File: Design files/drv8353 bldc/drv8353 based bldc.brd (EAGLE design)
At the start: 127 x 127 mm, 112 parts, among them IC1 DRV8353RSRGZT, J3 2X6 FEMALE, J4 B06B-HCMKK

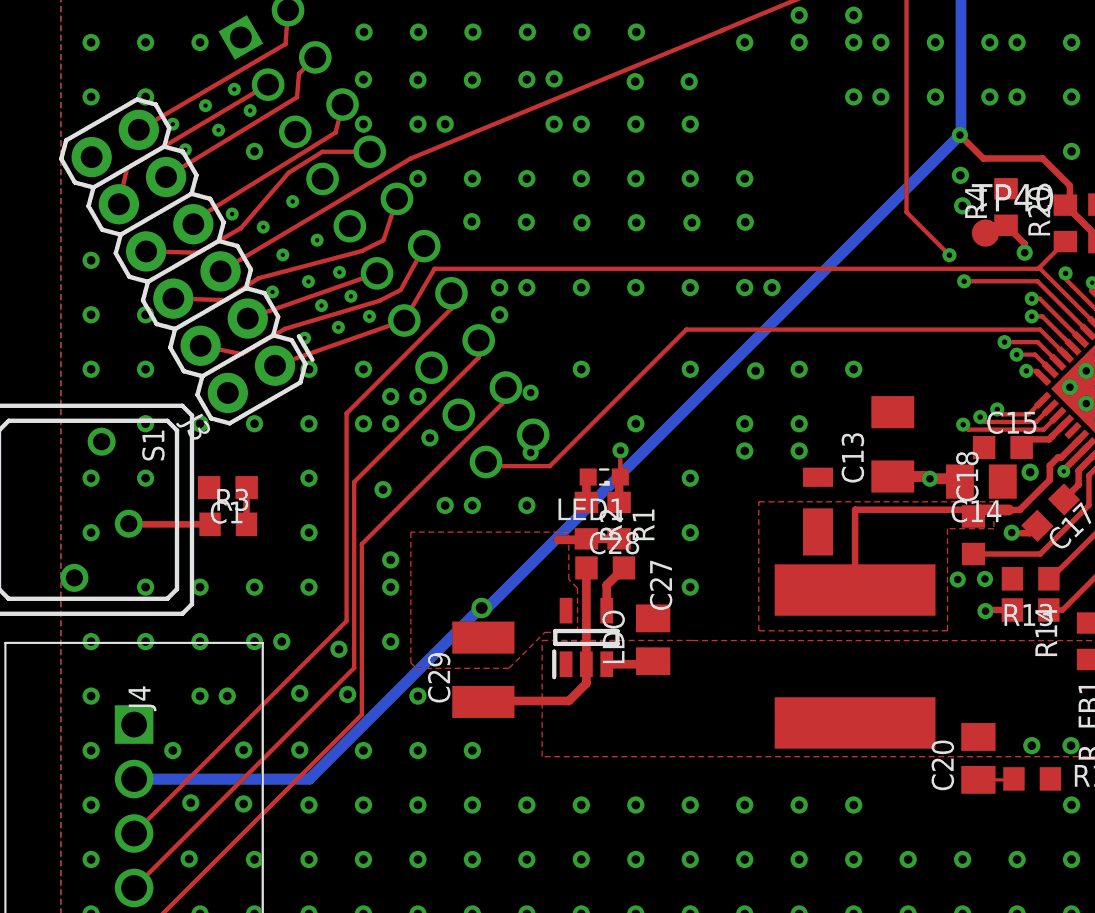
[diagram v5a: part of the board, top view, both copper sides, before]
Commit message: slight change to 3v3 ldo
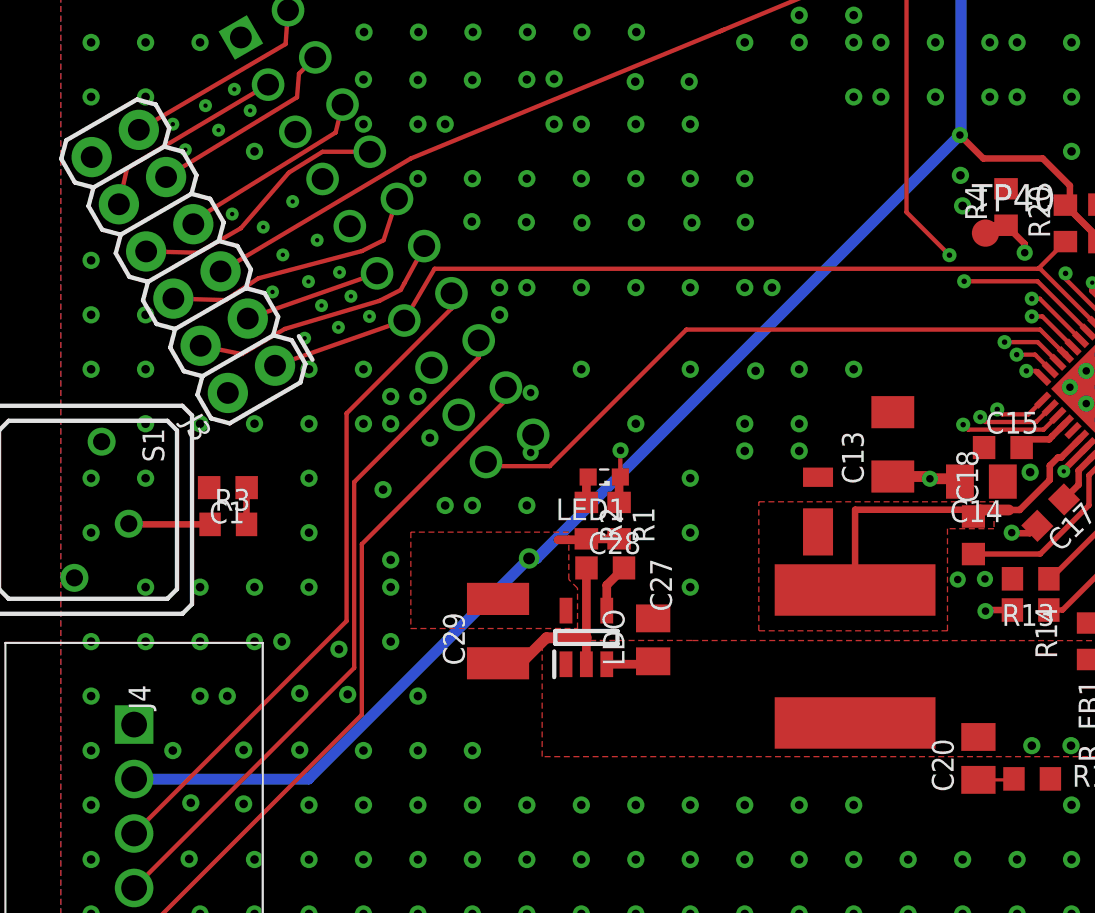
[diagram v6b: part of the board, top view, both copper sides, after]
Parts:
- moved C29 1.93 mm to (24.1, 70.3)
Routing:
- net N$5: track 10.6 -> 9.11 mm
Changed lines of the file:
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@@
 <?xml version="1.0" encoding="utf-8"?>
 <!DOCTYPE eagle SYSTEM "eagle.dtd">
-<eagle version="9.5.0">
+<eagle version="9.5.1">
 <drawing>
 <settings>
@@
 <layers>
 <layer number="1" name="Top" color="4" fill="1" visible="yes" active="yes"/>
-<layer number="2" name="Route2" color="16" fill="1" visible="no" active="yes"/>
+<layer number="2" name="Route2" color="16" fill="1" visible="yes" active="yes"/>
 <layer number="3" name="Route3" color="17" fill="1" visible="no" active="no"/>
 <layer number="4" name="Route4" color="18" fill="1" visible="no" active="no"/>
@@
 <layer number="13" name="Route13" color="21" fill="1" visible="no" active="no"/>
 <layer number="14" name="Route14" color="22" fill="1" visible="no" active="no"/>
-<layer number="15" name="Route15" color="23" fill="1" visible="no" active="yes"/>
-<layer number="16" name="Bottom" color="1" fill="1" visible="no" active="yes"/>
+<layer number="15" name="Route15" color="23" fill="1" visible="yes" active="yes"/>
+<layer number="16" name="Bottom" color="1" fill="1" visible="yes" active="yes"/>
 <layer number="17" name="Pads" color="2" fill="1" visible="yes" active="yes"/>
 <layer number="18" name="Vias" color="2" fill="1" visible="yes" active="yes"/>
@@
 <attribute name="SPICEPREFIX" value="C" x="72.2346" y="-49.9038" size="1.778" layer="27" display="off"/>
 </element>
-<element name="C29" library="rcl" library_urn="urn:adsk.eagle:library:334" package="C1210K" package3d_urn="urn:adsk.eagle:package:23683/2" value="4.7 uF" x="23.3698" y="68.5374" smashed="yes" rot="R90">
-<attribute name="NAME" x="21.8198" y="66.9374" size="1.016" layer="25" rot="R90"/>
-<attribute name="POPULARITY" value="0" x="123.6998" y="110.4474" size="1.778" layer="27" rot="R90" display="off"/>
-<attribute name="SPICEPREFIX" value="C" x="123.6998" y="110.4474" size="1.778" layer="27" rot="R90" display="off"/>
+<element name="C29" library="rcl" library_urn="urn:adsk.eagle:library:334" package="C1210K" package3d_urn="urn:adsk.eagle:package:23683/2" value="4.7 uF" x="24.0556" y="70.3408" smashed="yes" rot="R90">
+<attribute name="NAME" x="22.5056" y="68.7408" size="1.016" layer="25" rot="R90"/>
+<attribute name="POPULARITY" value="0" x="124.3856" y="112.2508" size="1.778" layer="27" rot="R90" display="off"/>
+<attribute name="SPICEPREFIX" value="C" x="124.3856" y="112.2508" size="1.778" layer="27" rot="R90" display="off"/>
 </element>
 <element name="C30" library="rcl" library_urn="urn:adsk.eagle:library:334" package="C1206" package3d_urn="urn:adsk.eagle:package:23618/2" value="1uF" x="79.2208" y="97.1468" smashed="yes" rot="R180">
@@
 <wire x1="31.2898" y1="68.9334" x2="31.1508" y2="68.7944" width="0.4064" layer="1"/>
 <wire x1="31.1508" y1="68.7944" x2="29.1258" y2="68.7944" width="0.4064" layer="1"/>
-<wire x1="29.1258" y1="68.7944" x2="27.2258" y2="68.7944" width="0" layer="19" extent="1-1"/>
 </signal>
 <signal name="FB">
@@
 <contactref element="IC1" pad="26"/>
 <polygon width="0.127" layer="1" thermals="no">
-<vertex x="24.5618" y="68.6054"/>
-<vertex x="26.2382" y="70.2818"/>
-<vertex x="27.7622" y="70.2818"/>
+<vertex x="19.9898" y="70.4596"/>
+<vertex x="27.7622" y="70.4596"/>
 <vertex x="27.7622" y="72.3392"/>
 <vertex x="27.3558" y="72.7456"/>
 <vertex x="27.3558" y="74.9554"/>
 <vertex x="19.9898" y="74.9554"/>
-<vertex x="19.9898" y="68.8594"/>
-<vertex x="20.2438" y="68.6054"/>
 </polygon>
 <contactref element="J4" pad="2"/>
-<wire x1="7.0848" y1="63.4418" x2="15.2648" y2="63.4418" width="0.508" layer="16"/>
-<wire x1="23.241" y1="71.418" x2="15.2648" y2="63.4418" width="0.508" layer="16"/>
-<wire x1="23.241" y1="71.418" x2="23.2918" y2="71.418" width="0.508" layer="16"/>
-<via x="23.2918" y="71.418" extent="1-16" drill="0.55"/>
-<wire x1="45.6438" y1="93.516" x2="23.5458" y2="71.418" width="0.508" layer="16"/>
-<wire x1="23.2918" y1="71.418" x2="23.5458" y2="71.418" width="0.508" layer="16"/>
+<wire x1="7.0848" y1="63.4418" x2="15.214" y2="63.4418" width="0.508" layer="16"/>
+<wire x1="25.5016" y1="73.7294" x2="15.214" y2="63.4418" width="0.508" layer="16"/>
+<via x="25.5016" y="73.7294" extent="1-16" drill="0.55"/>
+<wire x1="45.6438" y1="93.516" x2="25.8572" y2="73.7294" width="0.508" layer="16"/>
+<wire x1="25.5016" y1="73.7294" x2="25.8572" y2="73.7294" width="0.508" layer="16"/>
 <wire x1="45.6438" y1="93.516" x2="45.6438" y2="118.5926" width="0.508" layer="16"/>
 <wire x1="48.387" y1="121.3358" x2="45.6438" y2="118.5926" width="0.508" layer="16"/>
@@
 <contactref element="C28" pad="1"/>
 <contactref element="C29" pad="1"/>
-<wire x1="28.1758" y1="68.7944" x2="28.1758" y2="73.2824" width="0.4064" layer="1"/>
+<wire x1="28.1758" y1="68.7944" x2="28.1758" y2="70.0278" width="0.4064" layer="1"/>
+<wire x1="28.1758" y1="70.0278" x2="28.1758" y2="73.2824" width="0.4064" layer="1"/>
 <wire x1="28.1758" y1="73.2824" x2="28.1796" y2="73.2862" width="0.4064" layer="1"/>
-<wire x1="23.3698" y1="67.0374" x2="23.4138" y2="67.0814" width="0.4064" layer="1"/>
-<wire x1="27.3558" y1="67.0814" x2="23.4138" y2="67.0814" width="0.4064" layer="1"/>
-<wire x1="27.3558" y1="67.0814" x2="28.1758" y2="67.9014" width="0.4064" layer="1"/>
-<wire x1="28.1758" y1="67.9014" x2="28.1758" y2="68.7944" width="0.4064" layer="1"/>
+<wire x1="24.0556" y1="68.8408" x2="25.1224" y2="68.8408" width="0.508" layer="1"/>
+<wire x1="26.3094" y1="70.0278" x2="25.1224" y2="68.8408" width="0.508" layer="1"/>
+<wire x1="26.3094" y1="70.0278" x2="28.1758" y2="70.0278" width="0.508" layer="1"/>
 </signal>
 <signal name="N$13">

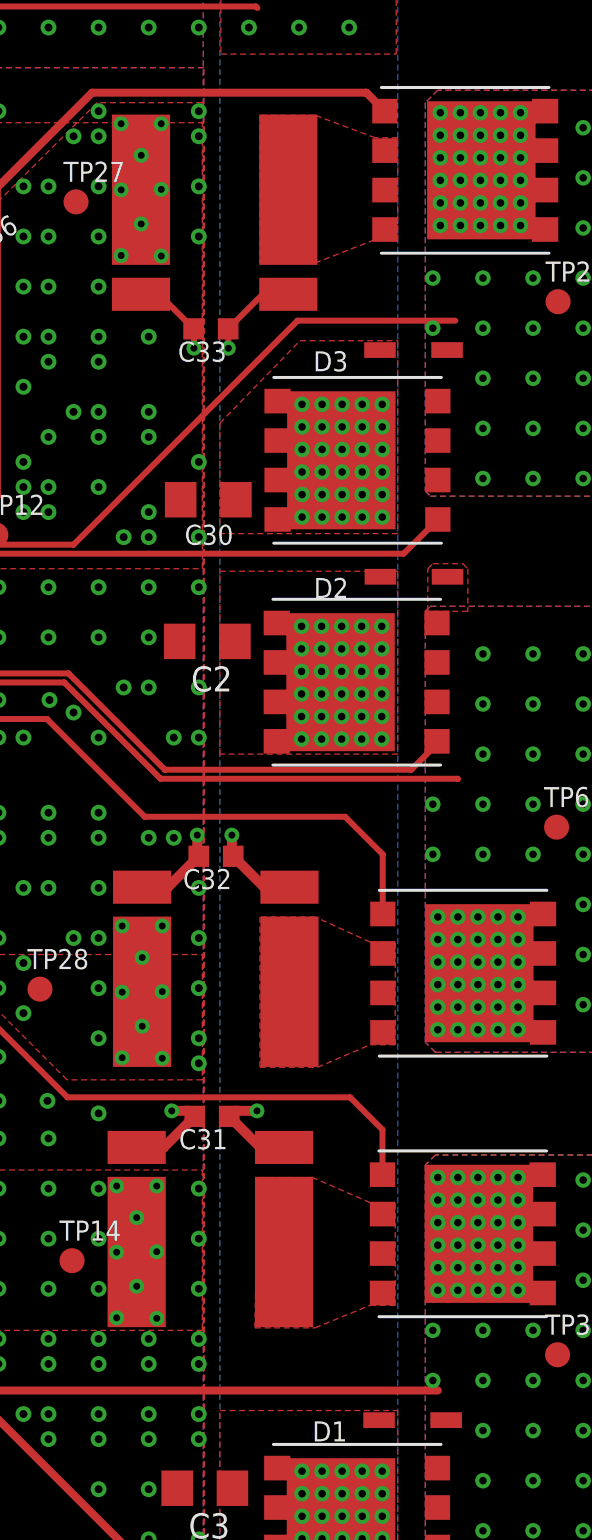
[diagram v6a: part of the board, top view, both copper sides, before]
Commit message: added low side flybacks
added low side flybacks
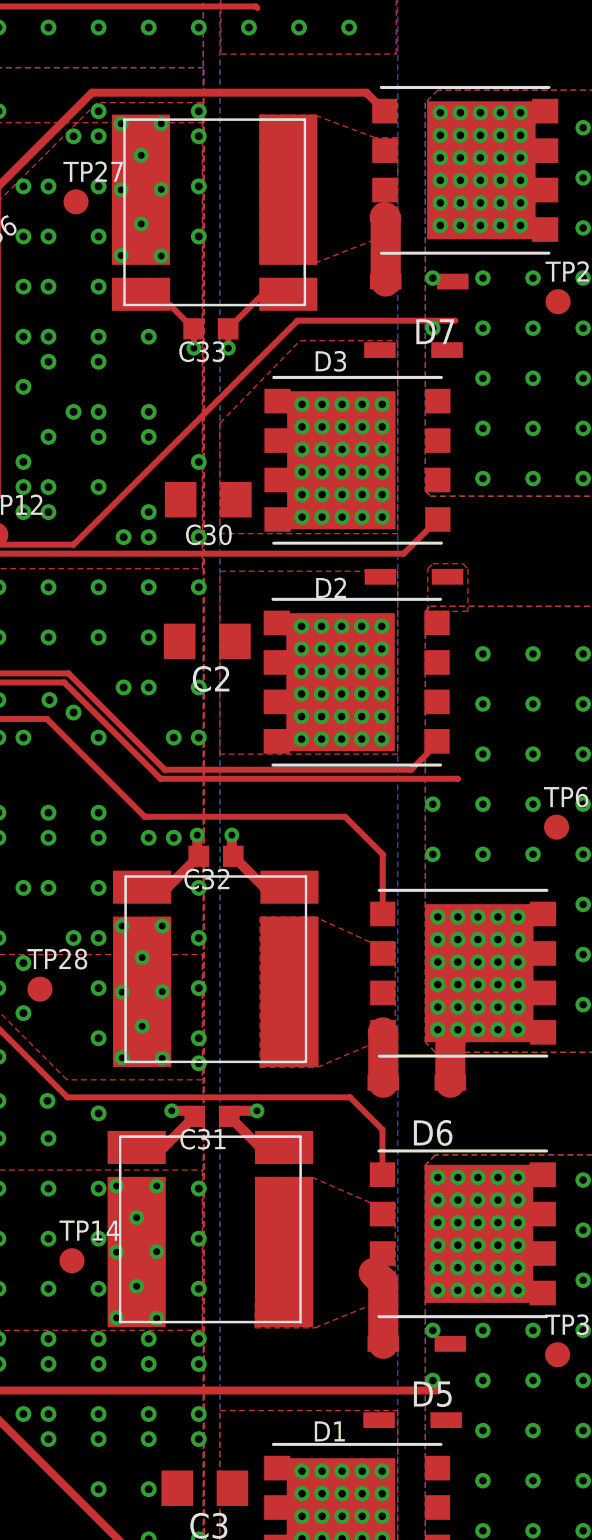
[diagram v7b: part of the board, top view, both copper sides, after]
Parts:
- added D5, D6, D7: (no value), REV BLDC:SOD123
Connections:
- net APHASE: now also D5.1
- net BPHASE: now also D6.1
- net CPHASE: now also D7.1
- net N$22: now also D6.2
- net N$24: now also D5.2
- net N$27: now also D7.2
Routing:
- net N$24: track 0.00 -> 3.81 mm
- net N$27: track 0.00 -> 3.30 mm
- net BPHASE: track 129.7 -> 132.5 mm
- net N$22: track 0.00 -> 2.57 mm
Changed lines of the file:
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@@
 <?xml version="1.0" encoding="utf-8"?>
 <!DOCTYPE eagle SYSTEM "eagle.dtd">
-<eagle version="9.5.1">
+<eagle version="9.5.0">
 <drawing>
 <settings>
@@
 <attribute name="VALUE" x="55.8546" y="118.2116" size="0.0254" layer="27"/>
 </element>
+<element name="D5" library="REV BLDC" package="SOD123" package3d_urn="urn:adsk.eagle:package:26308/2" value="" x="89.789" y="54.356" smashed="yes" rot="R180">
+<attribute name="NAME" x="91.694" y="52.451" size="1.27" layer="25" rot="R180"/>
+<attribute name="POPULARITY" value="0" x="89.789" y="54.356" size="1.778" layer="27" rot="R180" display="off"/>
+<attribute name="VALUE" x="91.694" y="57.531" size="1.27" layer="27" rot="R180"/>
+</element>
+<element name="D6" library="REV BLDC" package="SOD123" package3d_urn="urn:adsk.eagle:package:26308/2" value="" x="89.789" y="67.5894" smashed="yes" rot="R180">
+<attribute name="NAME" x="91.694" y="65.6844" size="1.27" layer="25" rot="R180"/>
+<attribute name="POPULARITY" value="0" x="89.789" y="67.5894" size="1.778" layer="27" rot="R180" display="off"/>
+<attribute name="VALUE" x="91.694" y="70.7644" size="1.27" layer="27" rot="R180"/>
+</element>
+<element name="D7" library="REV BLDC" package="SOD123" package3d_urn="urn:adsk.eagle:package:26308/2" value="" x="89.916" y="108.204" smashed="yes" rot="R180">
+<attribute name="NAME" x="91.821" y="106.299" size="1.27" layer="25" rot="R180"/>
+<attribute name="POPULARITY" value="0" x="89.916" y="108.204" size="1.778" layer="27" rot="R180" display="off"/>
+<attribute name="VALUE" x="91.821" y="111.379" size="1.27" layer="27" rot="R180"/>
+</element>
 </elements>
 <signals>
@@
 <wire x1="64.7954" y1="72.7356" x2="64.3736" y2="72.7356" width="0.3048" layer="1"/>
 <wire x1="64.3736" y1="72.7356" x2="64.3128" y2="72.7964" width="0.3048" layer="1"/>
+<contactref element="D5" pad="1"/>
 </signal>
 <signal name="BPHASE">
@@
 <wire x1="62.0776" y1="87.3762" x2="62.0776" y2="87.7316" width="0.3048" layer="1"/>
 <wire x1="62.0776" y1="87.7316" x2="62.23" y2="87.884" width="0.3048" layer="1"/>
+<contactref element="D6" pad="1"/>
+<wire x1="91.489" y1="67.5894" x2="91.489" y2="69.899" width="1.524" layer="1"/>
+<wire x1="91.489" y1="69.899" x2="91.8718" y2="70.2818" width="1.524" layer="1"/>
 </signal>
 <signal name="CPHASE">
@@
 <wire x1="68.453" y1="95.3606" x2="68.453" y2="94.9198" width="0.3048" layer="1"/>
 <wire x1="68.453" y1="94.9198" x2="68.4022" y2="94.869" width="0.3048" layer="1"/>
+<contactref element="D7" pad="1"/>
 </signal>
 <signal name="N$15">
@@
 </polygon>
 <contactref element="U$3" pad="I2"/>
+<contactref element="D5" pad="2"/>
+<wire x1="88.089" y1="54.356" x2="88.089" y2="57.4784" width="1.524" layer="1"/>
+<wire x1="88.089" y1="57.4784" x2="87.6046" y2="57.9628" width="1.524" layer="1"/>
 </signal>
 <signal name="N$22">
@@
 </polygon>
 <contactref element="U$4" pad="I2"/>
+<contactref element="D6" pad="2"/>
+<wire x1="88.0658" y1="70.1468" x2="88.089" y2="70.1236" width="1.524" layer="1"/>
+<wire x1="88.089" y1="70.1236" x2="88.089" y2="67.5894" width="1.524" layer="1"/>
 </signal>
 <signal name="N$27">
@@
 </polygon>
 <contactref element="U$5" pad="I1"/>
+<contactref element="D7" pad="2"/>
+<wire x1="88.216" y1="108.204" x2="88.216" y2="111.428" width="1.524" layer="1"/>
+<wire x1="88.216" y1="111.428" x2="88.1634" y2="111.4806" width="1.524" layer="1"/>
 </signal>
 <signal name="PGND">
